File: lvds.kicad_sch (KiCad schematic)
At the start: 87 parts, among them J15 Conn_FFC_Amphenol_62684-40210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

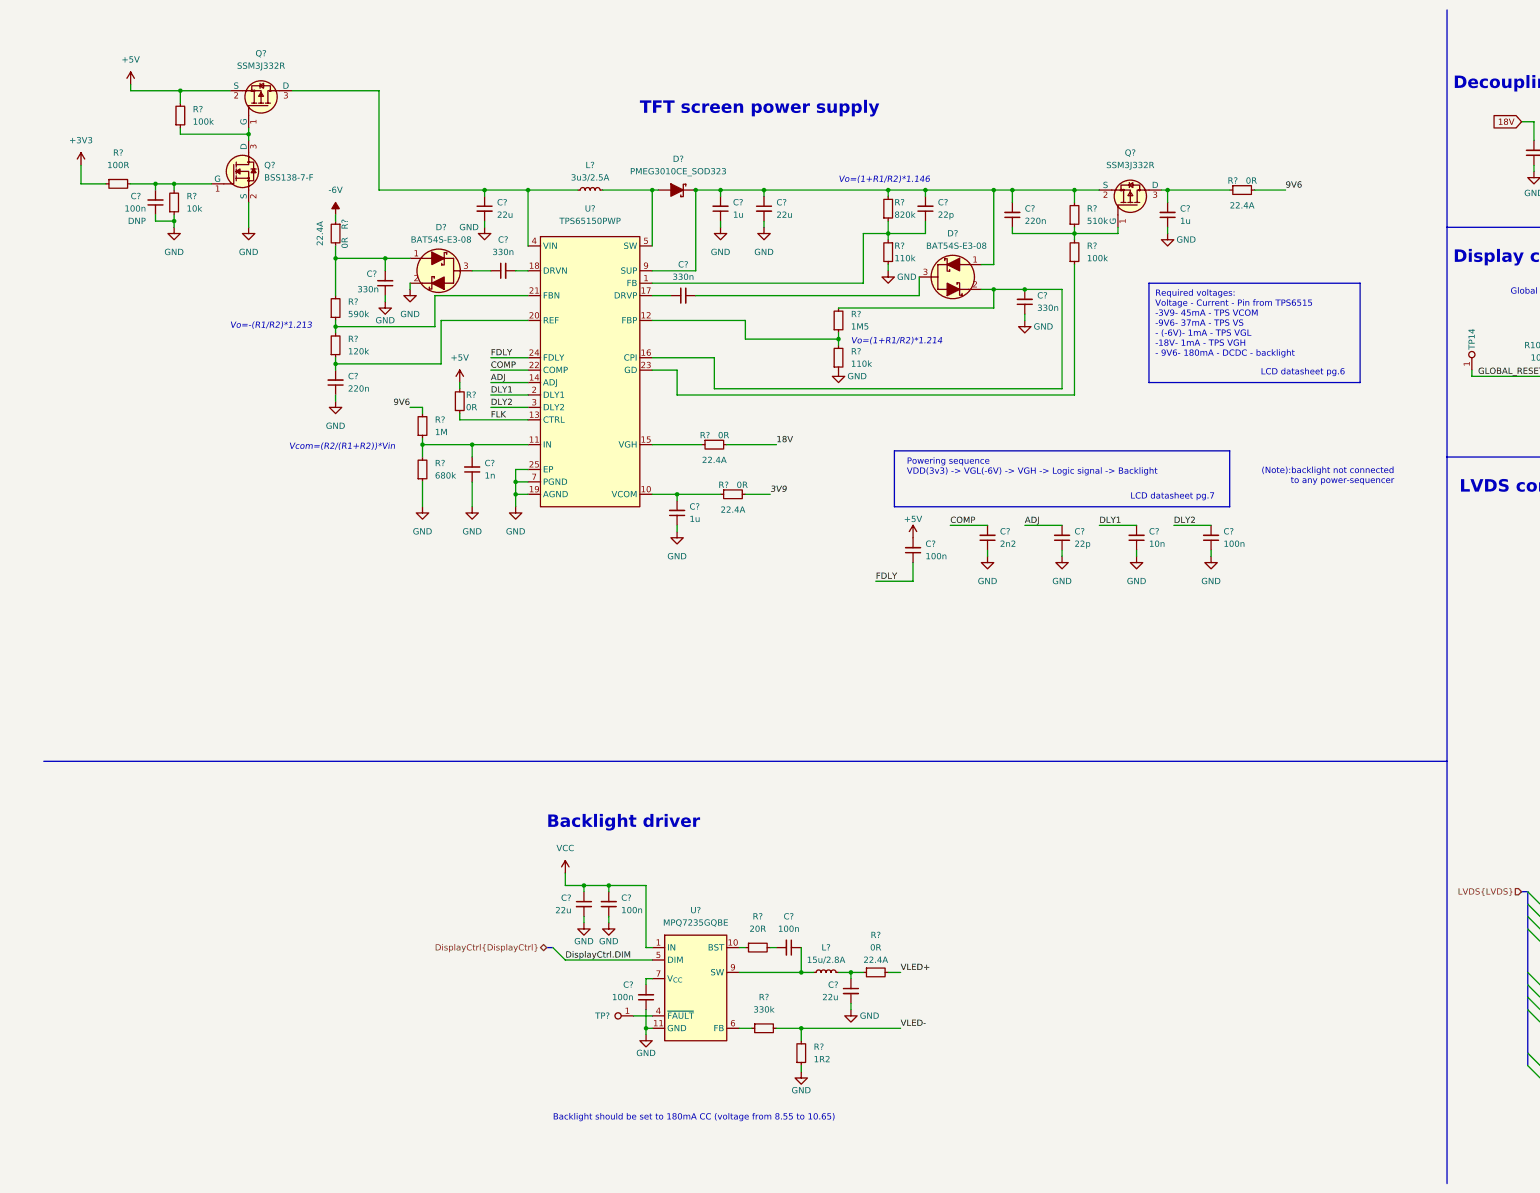
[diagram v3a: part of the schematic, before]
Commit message: [#54231] Update power sequencing for LVDS display
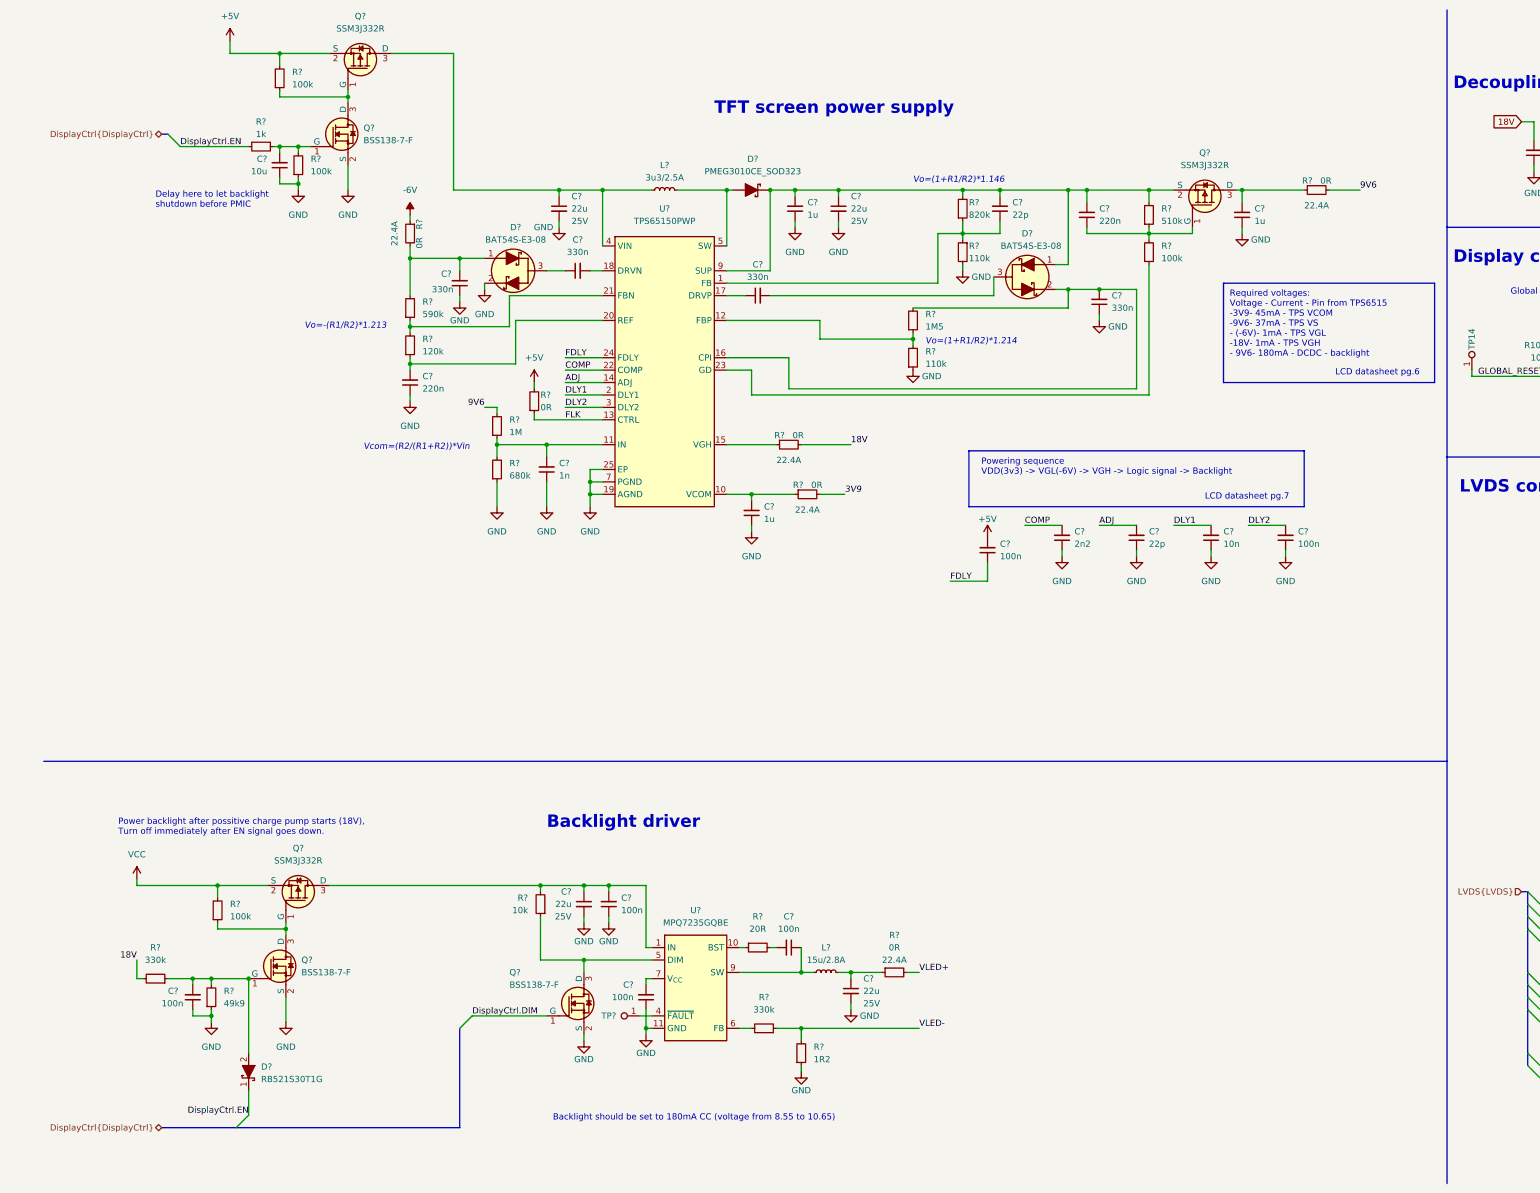
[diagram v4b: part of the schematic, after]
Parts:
- removed C?: C_100n_0402, antmicro-footprints:C_0402_1005Metric, symbol antmicroCapacitors0402:C_100n_0402
- removed R?: R_10k_0402, antmicro-footprints:R_0402_1005Metric, symbol antmicroResistors0402:R_10k_0402
- removed R?: R_100R_0402, antmicro-footprints:R_0402_1005Metric, symbol antmicroResistors0402:R_100R_0402
- added C?: C_10u_0402, antmicro-footprints:C_0402_1005Metric, symbol antmicroCapacitors0402:C_10u_0402
- added C?: C_100n_0402, antmicro-footprints:C_0402_1005Metric, symbol antmicroCapacitors0402:C_100n_0402
- added D?: RB521S30T1G, antmicro-footprints:SOD-523, symbol antmicroDiodesRectifiersSingle:RB521S30T1G
- added Q? (x2): BSS138-7-F, antmicro-footprints:SOT-23-3, symbol antmicroTransistorsFETsMOSFETsSingle:BSS138-7-F
- added Q?: SSM3J332R, antmicro-footprints:SOT-23-3, symbol antmicroTransistorsFETsMOSFETsSingle:SSM3J332R
- added R? (x2): R_100k_0402, antmicro-footprints:R_0402_1005Metric, symbol antmicroResistors0402:R_100k_0402
- added R?: R_1k_0402, antmicro-footprints:R_0402_1005Metric, symbol antmicroResistors0402:R_1k_0402
- added R?: R_10k_0402, antmicro-footprints:R_0402_1005Metric, symbol antmicroResistors0402:R_10k_0402
- added R?: R_330k_0402, antmicro-footprints:R_0402_1005Metric, symbol antmicroResistors0402:R_330k_0402
- added R?: R_49k9_0402, antmicro-footprints:R_0402_1005Metric, symbol antmicroResistors0402:R_49k9_0402
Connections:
- net 18V: now also R?.2
- net DisplayCtrl.DIM: now also Q?.1 (G); no longer U?.5 (DIM)
- net DisplayCtrl.EN: now also D?.1, R?.1
- net GND: now also C?.1, C?.1, Q?.2 (S), Q?.2 (S), R?.1, R?.1
- net VCC: now also Q?.2 (S), R?.2; no longer C?.1, C?.2, U?.1 (IN), U?.2 (IN)
- net VLED-: now also R?.1; no longer R?.2
- net at R?.1: now also C?.2, D?.2, Q?.1 (G), R?.2; no longer U?.6 (FB)
- net at Q?.1 (G): now also C?.2, R?.2, R?.2
- new net: Q?.1 (G), Q?.3 (D), R?.1
- new net: Q?.3 (D), R?.1, U?.5 (DIM)
- new net: C?.1, C?.2, Q?.3 (D), R?.2, U?.1 (IN), U?.2 (IN)
- new net: R?.2, U?.6 (FB)
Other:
- note added: "Delay here to let backlight shutdown before PMIC"
- note added: "Power backlight after possitive charge pump starts (18V), Turn off immediately after EN signal goes down."
- note removed: "(Note):backlight not connected to any power-sequencer"
- moved on the sheet: C?, D?, L?, Q?, R?, TP?, U?

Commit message: [#54231] Clean power supply for LVDS display
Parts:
- removed C? (x4): C_330n_0603, antmicro-footprints:C_0603_1608Metric, symbol antmicroCapacitors0603:C_330n_0603
- added C? (x4): C_1u_0402, antmicro-footprints:C_0402_1005Metric, symbol antmicroCapacitors0402:C_1u_0402
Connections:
- net GND: now also C?.1, C?.1
- net at D?.1, R?.2, R?.2: now also C?.2
- net at U?.17 (DRVP): now also C?.2
- net at D?.3: now also C?.1
- net at D?.2, R?.2, U?.16 (CPI): now also C?.2
- net at D?.3: now also C?.2
- net at U?.18 (DRVN): now also C?.1
- net GLOBAL_RESET renamed RESET
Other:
- note added: "Boost (9.6V)"
- note added: "Display decoupling capacitors"
- note added: "Negative charge pump (-6V)"
- note added: "Positve charge pump (18V)"
- note added: "Required voltages: Voltage - Current - Pin from TPS6515 - 3V9- 45mA - TPS VCOM - 9V6- 37mA - TPS VS - (-6V)- 1mA - TPS VGL - 18V- 1mA - TPS VGH - VCC(9-15V)- 180mA - DCDC - backlight"
- note added: "VCom (3.9V)"
- note added: "Vo=(1+R1/R2)*1.146 = 9.69V"
- note added: "Vo=(1+R1/R2)*1.214 = 17.76V"
- note added: "Vo=-(R1/R2)*1.213 = -5.96V"
- note removed: "Decoupling capacitors"
- note removed: "Required voltages: Voltage - Current - Pin from TPS6515 -3V9- 45mA - TPS VCOM -9V6- 37mA - TPS VS - (-6V)- 1mA - TPS VGL -18V- 1mA - TPS VGH - 9V6- 180mA - DCDC - backlight"
- note removed: "Vo=(1+R1/R2)*1.146"
- note removed: "Vo=(1+R1/R2)*1.214"
- note removed: "Vo=-(R1/R2)*1.213"
- moved on the sheet: C?, D?, L?, Q?, R?, TP?, U?

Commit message: [#54474] Complete USB schematics
- merge sch usb&debug
- add USB/4xUART bridge
- add USB-PD managament
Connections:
- net GND: no longer C?.2, C?.2, C?.2, C?.2
- net at C?.2, C?.2, C?.2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: no longer C?.1
- net at C?.2, Q?.3 (D), R?.2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: no longer C?.1
- net at L?.2, R?.1: no longer C?.1
- net at L?.1, Q?.3 (D), U?.4 (VIN): no longer C?.1
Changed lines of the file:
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@@
     (pin "2")
   )
-  (symbol (lib_name "C_22u_25V_0805_1") (lib_id "antmicroCapacitorsmisc:C_22u_25V_0805") (at 173.99 196.85 270) (unit 1)
+  (symbol (lib_id "antmicroCapacitorsmisc:C_22u_25V_0805") (at 173.99 196.85 270) (unit 1)
     (in_bom yes) (on_board yes) (fields_autoplaced)
     (property "Reference" "C?" (id 0) (at 171.45 196.8562 90)
@@
       (effects (font (size 1.27 1.27)) (justify left bottom) hide)
     )
-    (pin "1")
-    (pin "2")
   )
   (symbol (lib_id "antmicroCapacitors0402:C_10u_0402") (at 60.96 46.99 90) (unit 1)
@@
     (pin "2")
   )
-  (symbol (lib_name "C_22u_25V_0805_1") (lib_id "antmicroCapacitorsmisc:C_22u_25V_0805") (at 175.26 50.8 90) (mirror x) (unit 1)
+  (symbol (lib_id "antmicroCapacitorsmisc:C_22u_25V_0805") (at 175.26 50.8 90) (mirror x) (unit 1)
     (in_bom yes) (on_board yes) (fields_autoplaced)
     (property "Reference" "C?" (id 0) (at 177.8 50.8062 90)
@@
       (effects (font (size 1.27 1.27)) (justify left bottom) hide)
     )
-    (pin "1")
-    (pin "2")
   )
   (symbol (lib_id "antmicropower:GND") (at 335.28 240.03 0) (unit 1)
@@
     (pin "3")
   )
-  (symbol (lib_name "C_22u_25V_0805_1") (lib_id "antmicroCapacitorsmisc:C_22u_25V_0805") (at 119.38 50.8 90) (mirror x) (unit 1)
+  (symbol (lib_id "antmicroCapacitorsmisc:C_22u_25V_0805") (at 119.38 50.8 90) (mirror x) (unit 1)
     (in_bom yes) (on_board yes) (fields_autoplaced)
     (property "Reference" "C?" (id 0) (at 121.92 50.8062 90)
@@
       (effects (font (size 1.27 1.27)) (justify left bottom) hide)
     )
-    (pin "1")
-    (pin "2")
   )
   (symbol (lib_id "antmicropower:GND") (at 317.5 45.72 0) (unit 1)
@@
     (pin "2")
   )
-  (symbol (lib_name "C_22u_25V_0805_1") (lib_id "antmicroCapacitorsmisc:C_22u_25V_0805") (at 228.6 214.63 90) (mirror x) (unit 1)
+  (symbol (lib_id "antmicroCapacitorsmisc:C_22u_25V_0805") (at 228.6 214.63 90) (mirror x) (unit 1)
     (in_bom yes) (on_board yes) (fields_autoplaced)
     (property "Reference" "C?" (id 0) (at 231.14 214.6362 90)
@@
       (effects (font (size 1.27 1.27)) (justify left bottom) hide)
     )
-    (pin "1")
-    (pin "2")
   )
   (symbol (lib_id "antmicroTestPoints:TP_0.75mm_SMD") (at 382.27 210.82 180) (unit 1)

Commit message: [#54474] Fix broken capacitor symbols
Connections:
- net GND: now also C?.2, C?.2, C?.2, C?.2
- net at C?.2, C?.2, C?.2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: now also C?.1
- net at L?.2, R?.1: now also C?.1
- net at C?.2, Q?.3 (D), R?.2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: now also C?.1
- net at L?.1, Q?.3 (D), U?.4 (VIN): now also C?.1
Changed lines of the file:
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@@
       (effects (font (size 1.27 1.27)) (justify left bottom) hide)
     )
+    (pin "1")
+    (pin "2")
   )
   (symbol (lib_id "antmicroCapacitors0402:C_10u_0402") (at 60.96 46.99 90) (unit 1)
@@
       (effects (font (size 1.27 1.27)) (justify left bottom) hide)
     )
-    (property "Footprint" "antmicro-footprints:C_0805_2012Metric" (id 2) (at 170.18 55.88 0)
-      (effects (font (size 1.524 1.524)) (justify left bottom) hide)
+    (property "Footprint" "antmicro-footprints:C_0805_2012Metric" (id 2) (at 187.96 71.12 0)
+      (effects (font (size 1.27 1.27) (thickness 0.15)) (justify left bottom) hide)
     )
-    (property "Datasheet" "https://product.samsungsem.com/mlcc/CL21A226MAYNNN.do" (id 3) (at 175.26 50.8 0)
-      (effects (font (size 1.27 1.27)) (justify left bottom) hide)
+    (property "Datasheet" "https://product.samsungsem.com/mlcc/CL21A226MAYNNN.do" (id 3) (at 190.5 71.12 0)
+      (effects (font (size 1.27 1.27) (thickness 0.15)) (justify left bottom) hide)
     )
-    (property "Manufacturer" "Samsung Electro-Mechanics" (id 4) (at 165.1 55.88 0)
-      (effects (font (size 1.524 1.524)) (justify left bottom) hide)
+    (property "Manufacturer" "Samsung Electro-Mechanics" (id 4) (at 195.58 71.12 0)
+      (effects (font (size 1.27 1.27) (thickness 0.15)) (justify left bottom) hide)
     )
-    (property "MPN" "CL21A226MAYNNNE" (id 5) (at 167.64 55.88 0)
-      (effects (font (size 1.524 1.524)) (justify left bottom) hide)
+    (property "MPN" "CL21A226MAYNNNE" (id 5) (at 193.04 71.12 0)
+      (effects (font (size 1.27 1.27) (thickness 0.15)) (justify left bottom) hide)
     )
     (property "Val" "22u" (id 6) (at 177.8 53.3462 90)
-      (effects (font (size 1.27 1.27)) (justify right))
+      (effects (font (size 1.27 1.27) (thickness 0.15)) (justify right))
     )
     (property "License" "Apache-2.0" (id 7) (at 198.12 71.12 0)
@@
       (effects (font (size 1.27 1.27)) (justify left bottom) hide)
     )
+    (pin "1")
+    (pin "2")
   )
   (symbol (lib_id "antmicropower:GND") (at 335.28 240.03 0) (unit 1)
@@
       (effects (font (size 1.27 1.27)) (justify left bottom) hide)
     )
+    (pin "1")
+    (pin "2")
   )
   (symbol (lib_id "antmicropower:GND") (at 317.5 45.72 0) (unit 1)
@@
       (effects (font (size 1.27 1.27)) (justify left bottom) hide)
     )
+    (pin "1")
+    (pin "2")
   )
   (symbol (lib_id "antmicroTestPoints:TP_0.75mm_SMD") (at 382.27 210.82 180) (unit 1)

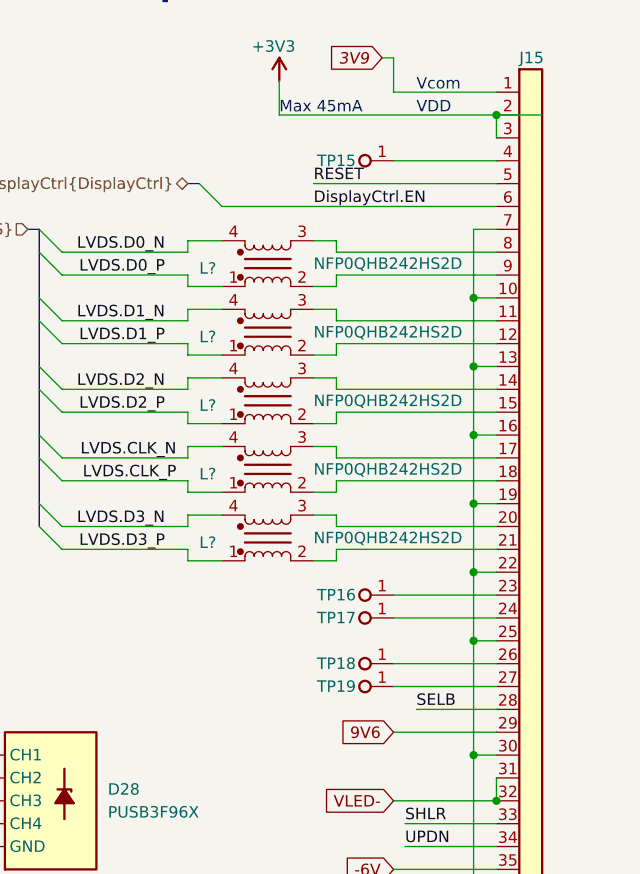
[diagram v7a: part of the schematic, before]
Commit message: [#54617] Clean labels: align & reduce duplicates
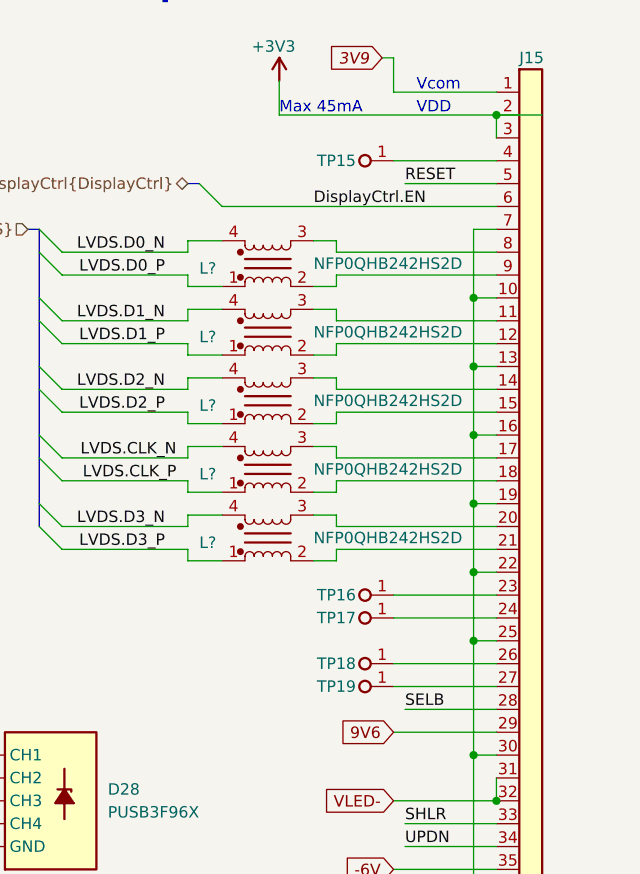
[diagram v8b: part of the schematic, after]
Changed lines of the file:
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@@
     (stroke (width 0) (type default) (color 0 0 0 0))
   )
-  (wire (pts (xy 384.81 190.5) (xy 393.7 190.5))
+  (wire (pts (xy 383.54 190.5) (xy 393.7 190.5))
     (stroke (width 0) (type default) (color 0 0 0 0))
   )
@@
     (stroke (width 0) (type default) (color 0 0 0 0))
   )
-  (wire (pts (xy 373.38 132.08) (xy 393.7 132.08))
+  (wire (pts (xy 383.54 132.08) (xy 393.7 132.08))
     (stroke (width 0) (type default) (color 0 0 0 0))
   )
@@
     (effects (font (size 1.27 1.27)) (justify left bottom))
   )
-  (label "RESET" (at 373.38 132.08 0)
+  (label "RESET" (at 383.54 132.08 0)
     (effects (font (size 1.27 1.27)) (justify left bottom))
   )
@@
     (effects (font (size 1.27 1.27)) (justify left bottom))
   )
-  (label "SELB" (at 384.81 190.5 0)
+  (label "SELB" (at 383.54 190.5 0)
     (effects (font (size 1.27 1.27)) (justify left bottom))
   )
